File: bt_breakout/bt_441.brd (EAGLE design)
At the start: 21.8 x 23 mm, 6 parts

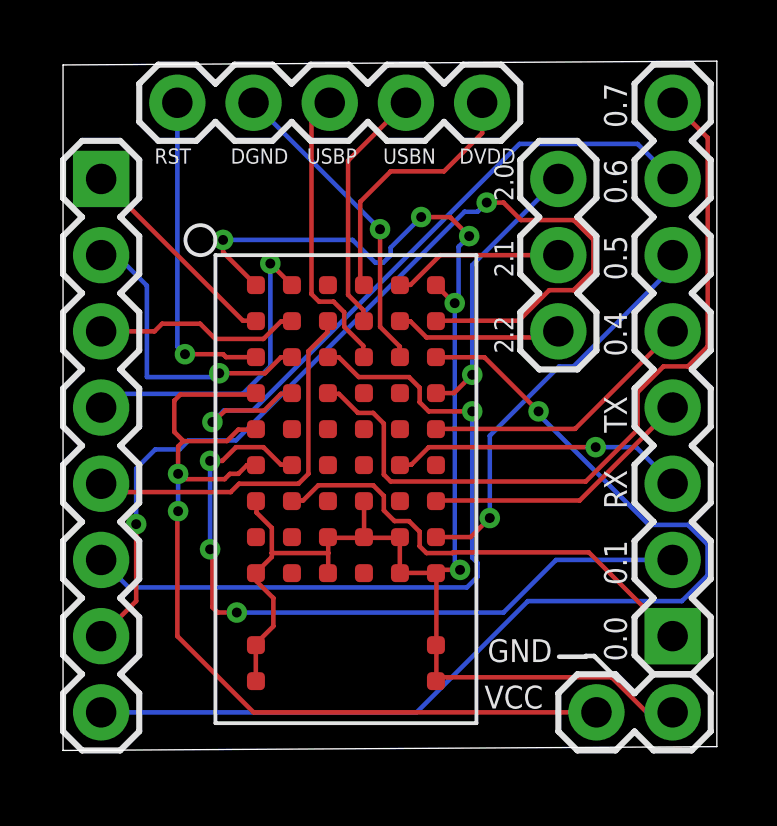
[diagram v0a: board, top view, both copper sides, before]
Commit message: Moved some text from bottom layer to top layer
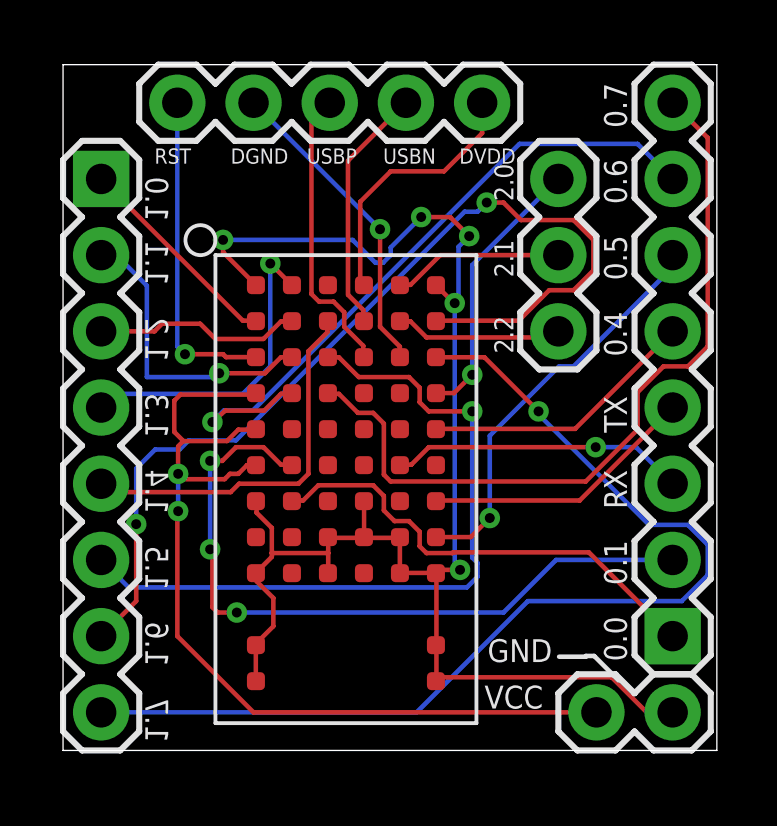
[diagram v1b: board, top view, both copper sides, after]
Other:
- board size 21.8 x 23 mm -> 21.8 x 22.9 mm
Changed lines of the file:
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@@
 <layer number="22" name="bPlace" color="7" fill="1" visible="yes" active="yes"/>
 <layer number="23" name="tOrigins" color="15" fill="1" visible="yes" active="yes"/>
-<layer number="24" name="bOrigins" color="15" fill="1" visible="yes" active="yes"/>
+<layer number="24" name="bOrigins" color="15" fill="1" visible="no" active="yes"/>
 <layer number="25" name="tNames" color="7" fill="1" visible="yes" active="yes"/>
 <layer number="26" name="bNames" color="7" fill="1" visible="yes" active="yes"/>
-<layer number="27" name="tValues" color="7" fill="1" visible="yes" active="yes"/>
-<layer number="28" name="bValues" color="7" fill="1" visible="yes" active="yes"/>
+<layer number="27" name="tValues" color="7" fill="1" visible="no" active="yes"/>
+<layer number="28" name="bValues" color="7" fill="1" visible="no" active="yes"/>
 <layer number="29" name="tStop" color="7" fill="3" visible="no" active="yes"/>
 <layer number="30" name="bStop" color="7" fill="6" visible="no" active="yes"/>
@@
 <layer number="109" name="ref-old" color="11" fill="1" visible="no" active="yes"/>
 <layer number="116" name="Patch_BOT" color="9" fill="4" visible="no" active="yes"/>
-<layer number="121" name="_tsilk" color="7" fill="1" visible="yes" active="yes"/>
-<layer number="122" name="_bsilk" color="7" fill="1" visible="yes" active="yes"/>
-<layer number="125" name="_tNames" color="7" fill="1" visible="yes" active="yes"/>
-<layer number="144" name="Drill_legend" color="7" fill="1" visible="yes" active="yes"/>
-<layer number="151" name="HeatSink" color="7" fill="1" visible="yes" active="yes"/>
-<layer number="199" name="Contour" color="7" fill="1" visible="yes" active="yes"/>
+<layer number="121" name="_tsilk" color="7" fill="1" visible="no" active="yes"/>
+<layer number="122" name="_bsilk" color="7" fill="1" visible="no" active="yes"/>
+<layer number="125" name="_tNames" color="7" fill="1" visible="no" active="yes"/>
+<layer number="144" name="Drill_legend" color="7" fill="1" visible="no" active="yes"/>
+<layer number="151" name="HeatSink" color="7" fill="1" visible="no" active="yes"/>
+<layer number="199" name="Contour" color="7" fill="1" visible="no" active="yes"/>
 <layer number="200" name="200bmp" color="1" fill="10" visible="no" active="yes"/>
-<layer number="201" name="201bmp" color="2" fill="10" visible="yes" active="yes"/>
-<layer number="202" name="202bmp" color="3" fill="10" visible="yes" active="yes"/>
-<layer number="203" name="203bmp" color="4" fill="10" visible="yes" active="yes"/>
-<layer number="204" name="204bmp" color="5" fill="10" visible="yes" active="yes"/>
-<layer number="205" name="205bmp" color="6" fill="10" visible="yes" active="yes"/>
-<layer number="206" name="206bmp" color="7" fill="10" visible="yes" active="yes"/>
-<layer number="207" name="207bmp" color="8" fill="10" visible="yes" active="yes"/>
-<layer number="208" name="208bmp" color="9" fill="10" visible="yes" active="yes"/>
-<layer number="209" name="209bmp" color="7" fill="1" visible="yes" active="yes"/>
-<layer number="210" name="210bmp" color="7" fill="1" visible="yes" active="yes"/>
-<layer number="211" name="211bmp" color="7" fill="1" visible="yes" active="yes"/>
-<layer number="212" name="212bmp" color="7" fill="1" visible="yes" active="yes"/>
-<layer number="213" name="213bmp" color="7" fill="1" visible="yes" active="yes"/>
-<layer number="214" name="214bmp" color="7" fill="1" visible="yes" active="yes"/>
-<layer number="215" name="215bmp" color="7" fill="1" visible="yes" active="yes"/>
-<layer number="216" name="216bmp" color="7" fill="1" visible="yes" active="yes"/>
+<layer number="201" name="201bmp" color="2" fill="10" visible="no" active="yes"/>
+<layer number="202" name="202bmp" color="3" fill="10" visible="no" active="yes"/>
+<layer number="203" name="203bmp" color="4" fill="10" visible="no" active="yes"/>
+<layer number="204" name="204bmp" color="5" fill="10" visible="no" active="yes"/>
+<layer number="205" name="205bmp" color="6" fill="10" visible="no" active="yes"/>
+<layer number="206" name="206bmp" color="7" fill="10" visible="no" active="yes"/>
+<layer number="207" name="207bmp" color="8" fill="10" visible="no" active="yes"/>
+<layer number="208" name="208bmp" color="9" fill="10" visible="no" active="yes"/>
+<layer number="209" name="209bmp" color="7" fill="1" visible="no" active="yes"/>
+<layer number="210" name="210bmp" color="7" fill="1" visible="no" active="yes"/>
+<layer number="211" name="211bmp" color="7" fill="1" visible="no" active="yes"/>
+<layer number="212" name="212bmp" color="7" fill="1" visible="no" active="yes"/>
+<layer number="213" name="213bmp" color="7" fill="1" visible="no" active="yes"/>
+<layer number="214" name="214bmp" color="7" fill="1" visible="no" active="yes"/>
+<layer number="215" name="215bmp" color="7" fill="1" visible="no" active="yes"/>
+<layer number="216" name="216bmp" color="7" fill="1" visible="no" active="yes"/>
 <layer number="217" name="217bmp" color="18" fill="1" visible="no" active="no"/>
 <layer number="218" name="218bmp" color="19" fill="1" visible="no" active="no"/>
@@
 <layer number="250" name="Descript" color="3" fill="1" visible="no" active="no"/>
 <layer number="251" name="SMDround" color="12" fill="11" visible="no" active="no"/>
-<layer number="254" name="cooling" color="7" fill="1" visible="yes" active="yes"/>
+<layer number="254" name="cooling" color="7" fill="1" visible="no" active="yes"/>
 </layers>
 <board>
 <plain>
-<wire x1="0" y1="0" x2="21.7934" y2="0.127" width="0" layer="20"/>
-<wire x1="21.7934" y1="0.127" x2="21.7934" y2="22.977" width="0" layer="20"/>
-<wire x1="21.7934" y1="22.977" x2="0" y2="22.85" width="0" layer="20"/>
-<wire x1="0" y1="22.85" x2="0" y2="0" width="0" layer="20"/>
+<wire x1="0" y1="0" x2="21.7934" y2="0" width="0" layer="20"/>
+<wire x1="21.7934" y1="0" x2="21.7934" y2="22.86" width="0" layer="20"/>
+<wire x1="21.7934" y1="22.86" x2="0" y2="22.86" width="0" layer="20"/>
+<wire x1="0" y1="22.86" x2="0" y2="0" width="0" layer="20"/>
 <text x="18.796" y="2.9718" size="0.762" layer="25" rot="R90">0.0</text>
 <text x="18.796" y="5.5118" size="0.762" layer="25" rot="R90">0.1</text>
@@
 <text x="18.796" y="18.2118" size="0.762" layer="25" rot="R90">0.6</text>
 <text x="18.796" y="20.7518" size="0.762" layer="25" rot="R90">0.7</text>
-<text x="3.5052" y="19.1262" size="0.762" layer="26" rot="MR270">1.0</text>
-<text x="3.5052" y="16.9926" size="0.762" layer="26" rot="MR270">1.1</text>
-<text x="3.5052" y="14.4526" size="0.762" layer="26" rot="MR270">1.2</text>
-<text x="3.5052" y="11.9126" size="0.762" layer="26" rot="MR270">1.3</text>
-<text x="3.5052" y="9.3726" size="0.762" layer="26" rot="MR270">1.4</text>
-<text x="3.5052" y="6.8326" size="0.762" layer="26" rot="MR270">1.5</text>
-<text x="3.5052" y="4.2926" size="0.762" layer="26" rot="MR270">1.6</text>
-<text x="3.5052" y="1.7526" size="0.762" layer="26" rot="MR270">1.7</text>
+<text x="3.5052" y="19.1262" size="0.762" layer="25" rot="MR270">1.0</text>
+<text x="3.5052" y="16.9926" size="0.762" layer="25" rot="MR270">1.1</text>
+<text x="3.5052" y="14.4526" size="0.762" layer="25" rot="MR270">1.2</text>
+<text x="3.5052" y="11.9126" size="0.762" layer="25" rot="MR270">1.3</text>
+<text x="3.5052" y="9.3726" size="0.762" layer="25" rot="MR270">1.4</text>
+<text x="3.5052" y="6.8326" size="0.762" layer="25" rot="MR270">1.5</text>
+<text x="3.5052" y="4.2926" size="0.762" layer="25" rot="MR270">1.6</text>
+<text x="3.5052" y="1.7526" size="0.762" layer="25" rot="MR270">1.7</text>
 <text x="13.208" y="19.558" size="0.508" layer="25">DVDD</text>
 <text x="10.668" y="19.558" size="0.508" layer="25">USBN</text>
